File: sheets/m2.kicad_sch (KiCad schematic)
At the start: 52 parts, among them CN1 EM92xx / RM520N M.2 Key-B (67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, Q1 2N7002, Q2 2N7002, Q3 2N7002, Q32 DMG3415U-7, Q4 2N7002, Q5 2N7002

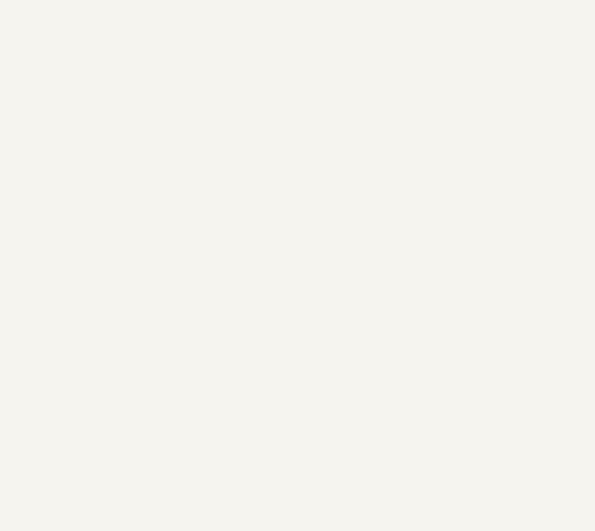
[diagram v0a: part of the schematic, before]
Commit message: sch: audit fixes — buck EN divider corners, 3V3-domain senses, spec §10 LEDs
F1 (critical): TPS565201 BUCK_EN divider (R40/R41) redesigned against the
datasheet's VENH/VENL/REN corners so the 3.3V buck actually starts once the
12V node is negotiated, without false-starting on pre-negotiation 5V VBUS.

F2 (medium): GP18/GP19 retargeted from the RP2040 sheet to the ethernet
sheet's existing 3.3V-domain PERST/CLKREQ shifter outputs; GP17 gets a new
BSS138 level-shift stage (Q40/R122) on m2, mirroring the Task 10 pattern.

F3 (minor): added the two spec §10 indicator LEDs (D29 12V/power, D30
PD-good) that were dropped during Task 4 and never restored.

check_nets.py all pass; ERC 0 errors / 800 warnings (was 788, full delta
accounted in docs/erc-waivers.md); netlist exports clean, no annotation
warnings.

Co-Authored-By: Claude Fable 5 <noreply@anthropic.com>
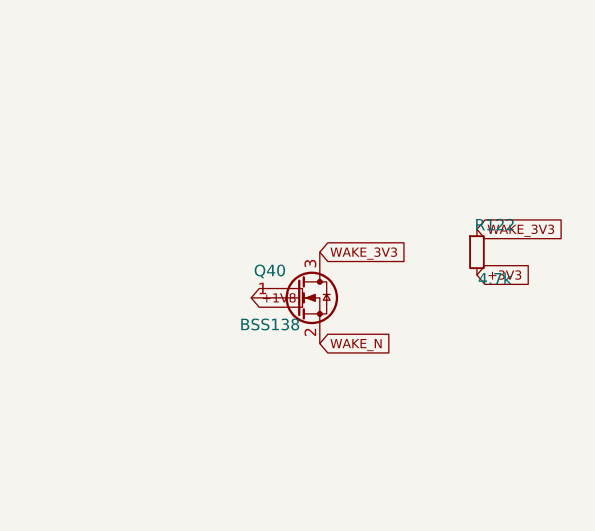
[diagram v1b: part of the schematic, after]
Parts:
- added Q40: BSS138, Package_TO_SOT_SMD:SOT-23, symbol Transistor_FET:BSS138
- added R122: 4.7k, Resistor_SMD:R_0603_1608Metric, symbol Device:R_Small
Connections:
- net +1V8: now also Q40.1 (G)
- net +3V3: now also R122.2
- net WAKE_N: now also Q40.2 (S)
- new net WAKE_3V3: Q40.3 (D), R122.1
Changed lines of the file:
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@@
+	)
+	(symbol
+		(lib_id "Transistor_FET:BSS138")
+		(at 320 265 0)
+		(unit 1)
+		(exclude_from_sim no)
+		(in_bom yes)
+		(on_board yes)
+		(dnp no)
+		(fields_autoplaced yes)
+		(property "Reference" "Q40" (at 317 262 0) (effects (font (size 1.27 1.27))))
+		(property "Value" "BSS138" (at 317 268 0) (effects (font (size 1.27 1.27))))
+		(property "Footprint" "Package_TO_SOT_SMD:SOT-23" (at 320 265 0) (hide yes) (effects (font (size 1.27 1.27))))
+		(property "Datasheet" "https://datasheet.lcsc.com/datasheet/pdf/4150e64aba6a4527a5b33f9c08ea7327.pdf?productCode=C8490" (at 320 265 0) (hide yes) (effects (font (size 1.27 1.27))))
+		(pin "1")
+		(pin "2")
+		(pin "3")
+		(instances
+			(project "sierra-to-usb"
+				(path "/f141b3c0-0a69-4819-acb0-dc32f46a3541/73117a4a-deaa-4ee3-9b76-9f9d022b6743"
+					(reference "Q40")
+					(unit 1)
+				)
+			)
+		)
+	)
+	(symbol
+		(lib_id "Device:R_Small")
+		(at 340 259.92 0)
+		(unit 1)
+		(exclude_from_sim no)
+		(in_bom yes)
+		(on_board yes)
+		(dnp no)
+		(fields_autoplaced yes)
+		(property "Reference" "R122" (at 342 256.92 0) (effects (font (size 1.27 1.27))))
+		(property "Value" "4.7k" (at 342 262.92 0) (effects (font (size 1.27 1.27))))
+		(property "Footprint" "Resistor_SMD:R_0603_1608Metric" (at 340 259.92 0) (hide yes) (effects (font (size 1.27 1.27))))
+		(property "Datasheet" "" (at 340 259.92 0) (hide yes) (effects (font (size 1.27 1.27))))
+		(pin "1")
+		(pin "2")
+		(instances
+			(project "sierra-to-usb"
+				(path "/f141b3c0-0a69-4819-acb0-dc32f46a3541/73117a4a-deaa-4ee3-9b76-9f9d022b6743"
+					(reference "R122")
+					(unit 1)
+				)
+			)
+		)
 	)
 	(symbol
@@
 		(property "Intersheetrefs" "${INTERSHEET_REFS}" (at 230.0 274.0 0) (effects (font (size 1.27 1.27))))
 	)
+	(global_label "+1V8"
+		(shape input)
+		(at 314.92 265.0 0)
+		(effects (font (size 1.016 1.016)) (justify left bottom))
+		(property "Intersheetrefs" "${INTERSHEET_REFS}" (at 314.92 265.0 0) (effects (font (size 1.27 1.27))))
+	)
+	(global_label "WAKE_N"
+		(shape input)
+		(at 322.54 270.08 0)
+		(effects (font (size 1.016 1.016)) (justify left bottom))
+		(property "Intersheetrefs" "${INTERSHEET_REFS}" (at 322.54 270.08 0) (effects (font (size 1.27 1.27))))
+	)
+	(global_label "WAKE_3V3"
+		(shape input)
+		(at 322.54 259.92 0)
+		(effects (font (size 1.016 1.016)) (justify left bottom))
+		(property "Intersheetrefs" "${INTERSHEET_REFS}" (at 322.54 259.92 0) (effects (font (size 1.27 1.27))))
+	)
+	(global_label "WAKE_3V3"
+		(shape input)
+		(at 340.0 257.38 0)
+		(effects (font (size 1.016 1.016)) (justify left bottom))
+		(property "Intersheetrefs" "${INTERSHEET_REFS}" (at 340.0 257.38 0) (effects (font (size 1.27 1.27))))
+	)
+	(global_label "+3V3"
+		(shape input)
+		(at 340.0 262.46 0)
+		(effects (font (size 1.016 1.016)) (justify left bottom))
+		(property "Intersheetrefs" "${INTERSHEET_REFS}" (at 340.0 262.46 0) (effects (font (size 1.27 1.27))))
+	)
 	(global_label "PERST_N"

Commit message: sch: footprints + assembly-split BOM fields
Task 14: bind real footprints to all 363 BOM symbols, add Assembly/LCSC/MPN/
Distributor properties to every symbol, and close the accumulated
footprint_link_issues ERC deferral (148 -> 0).

- New fp-lib-table + lib/sierra-to-usb.pretty/ (15 custom footprints
  authored from real manufacturer drawings: magjack, MHF4, SMA edge,
  nano-SIM, MFF2 eSIM, M.2 socket, bridge rectifier, 2x PoE flyback
  inductors, TPS23730 VQFN-45, FDMC2523P, FOD817 gull-wing DIP-4, SK6805
  LED, PoE transformer, and a corrected full-24-pin USB-C receptacle for
  J1 -- the previously-bound stock footprint only exposed 6 of 24 pins).
- Fixed ~120 bare/stale/wrong-library-prefix Footprint strings project-wide.
- Assembly split: 12 JLC rows (all LCSC-backed), 351 HAND rows (MPN +
  Distributor on every one). Disclosed flip: U30 (eSIM) JLC->HAND per
  sourcing.md's own no-LCSC-listing flag, overriding the task's shorthand.
- Carry-forwards closed: D30 series R 1k->560R, INA226 MSOP-10->VSSOP-10
  (+EP-VIA), R39/R44 Kelvin-route note, JP1-3 solder-jumper footprints,
  SW2 silk note, 42x 0402->0603 hand-solder upgrades.
- New tools/check_footprints.py gate: Footprint/Assembly presence, JLC=>LCSC,
  and footprint-pad-count >= symbol-pin-count (parsed from real .kicad_mod
  files + netlist pin lists).
- Recovered sheets/mcu.kicad_sch from a pre-existing uncommitted data-loss
  state (44 symbols missing vs the Task 13 gate-approved commit) before
  applying any Task 14 edits.

Verification: check_footprints.py all-pass, check_nets.py all-pass
(connectivity untouched), kicad-cli sch erc 0 errors.

Two pre-existing issues disclosed but not fixed here (out of footprint-
assignment scope, documented in docs/verification.md and
docs/erc-waivers.md): J1's now-corrected footprint was masking a Task-7
error, and 7 refs (Q20,Q22-25,Q30,Q31) use letter-pinned generic FET/BJT
symbols that will show unmatched pins at PCB import regardless of
footprint choice -- flagge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
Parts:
- C44, C45, C46: Assembly (none) -> HAND; Distributor (none) -> LCSC; MPN (none) -> Generic MLCC 470uF 0603 (Yageo/Murata/Samsung equiv, exact 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
- C47, C48, C49, C50, C51, C52: Assembly (none) -> HAND; Distributor (none) -> LCSC; MPN (none) -> Generic MLCC 10uF 0805 (Yageo/Murata/Samsung equiv, exact P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
- C53, C54, C55, C56, C57: footprint Capacitor_SMD:C_0402_1005Metric -> Capacitor_SMD:C_0603_1608Metric; Assembly (none) -> HAND; Distributor (none) -> LCSC; MPN (none) -> Generic MLCC 0.1uF 0402 (Yageo/Murata/Samsung equiv, exact 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
- CN1: footprint Connector_M.2:M.2_Key-B-SMD -> sierra-to-usb:M.2_Key-B-SMD_Socket_LOTES_APCI0105-P001A; Assembly (none) -> JLC; Distributor (none) -> LCSC; LCSC (none) -> C841658; MPN (none) -> LOTES APCI0105-P001A
- D19: Assembly (none) -> HAND; Distributor (none) -> LCSC; MPN (none) -> Generic blue 0603 LED (WWAN status, Yageo/Everlight equiv)
- JP1, JP2, JP3: footprint Jumper:SolderJumper-2_P1.3mm_Open_Circle -> Jumper:SolderJumper-2_P1.3mm_Open_RoundedPad1.0x1.5mm; Assembly (none) -> HAND; Distributor (none) -> N/A; MPN (none) -> N/A (solder-jumper PCB feature, no discrete part)
- Q1, Q2, Q3, Q4, Q5: Assembly (none) -> HAND; Distributor (none) -> LCSC; LCSC (none) -> C8545; MPN (none) -> 2N7002
- Q32: Assembly (none) -> HAND; Distributor (none) -> LCSC; LCSC (none) -> C96616; MPN (none) -> Diodes DMG3415U-7
- Q40: Assembly (none) -> HAND; Distributor (none) -> LCSC; LCSC (none) -> C8490; MPN (none) -> LRC LBSS138LT1G
- R122: Assembly (none) -> HAND; Distributor (none) -> LCSC; MPN (none) -> Yageo RC0603JR-074K7L
- R51, R52, R54, R56, R58, R62, R63, R68: Assembly (none) -> HAND; Distributor (none) -> LCSC; MPN (none) -> Yageo RC0603JR-07100KL
- R53, R55, R57, R64, R65, R66: Assembly (none) -> HAND; Distributor (none) -> LCSC; MPN (none) -> Yageo RC0603JR-0710KL
- R59: Assembly (none) -> HAND; Distributor (none) -> LCSC; LCSC (none) -> C126359; MPN (none) -> Yageo RC0603FR-0733KL
- R60: Assembly (none) -> HAND; Distributor (none) -> LCSC; MPN (none) -> Yageo RC0603FR-0718KL (pattern-inferred, not live-verified)
- R61: Assembly (none) -> HAND; Distributor (none) -> LCSC; MPN (none) -> Yageo RC0603JR-07330RL
- R67: Assembly (none) -> HAND; Distributor (none) -> LCSC; MPN (none) -> Yageo RC0603JR-071KL
- TP1, TP2, TP3, TP4, TP5, TP6, TP7, TP8, TP9: Assembly (none) -> HAND; Distributor (none) -> N/A; MPN (none) -> N/A (bare copper test pad, no discrete part)
